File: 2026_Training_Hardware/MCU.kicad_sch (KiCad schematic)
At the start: 2 parts, among them J1 RJ45_LED_Shielded, U1 Teensy4.1_DEV-16771

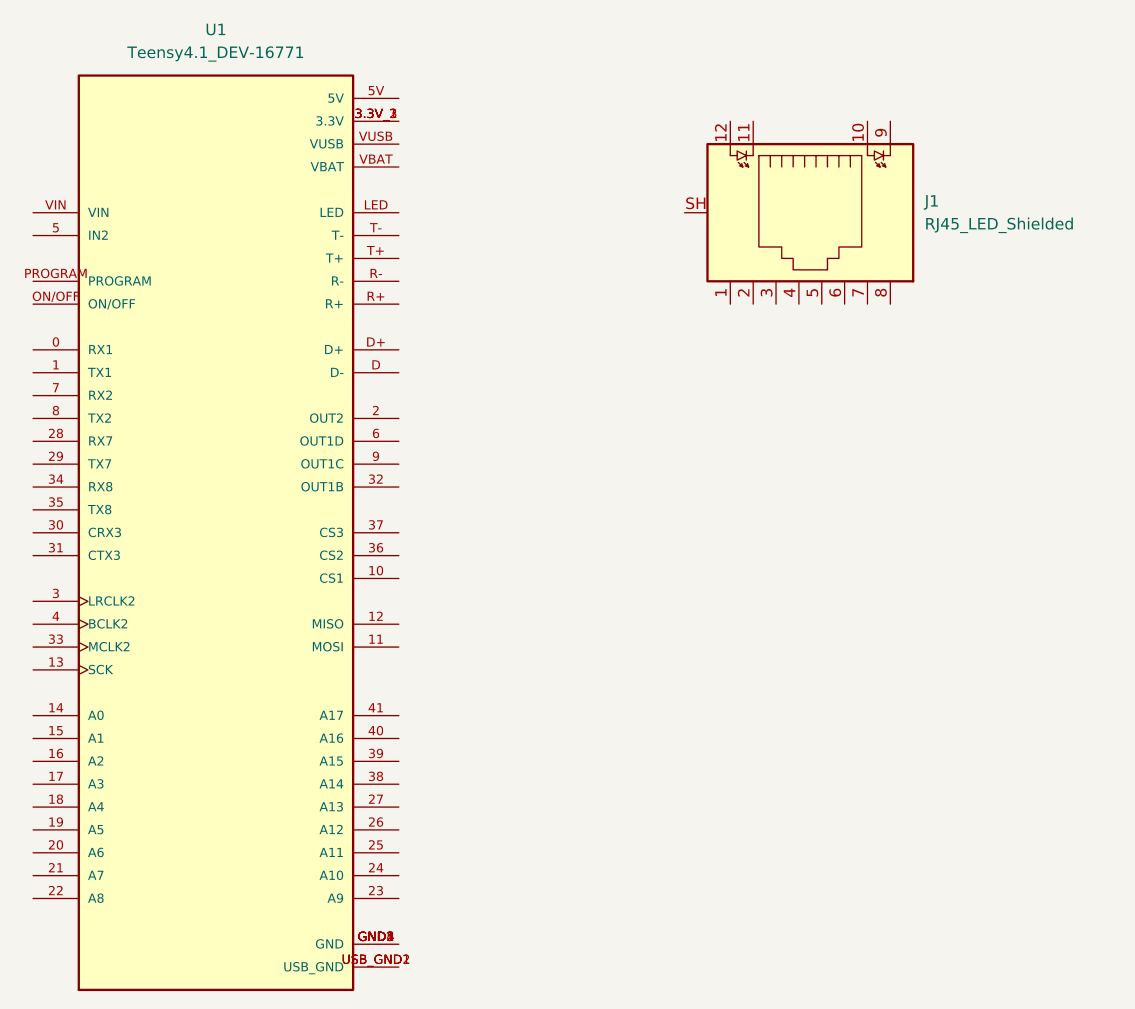
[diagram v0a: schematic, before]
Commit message: Add Ethernet
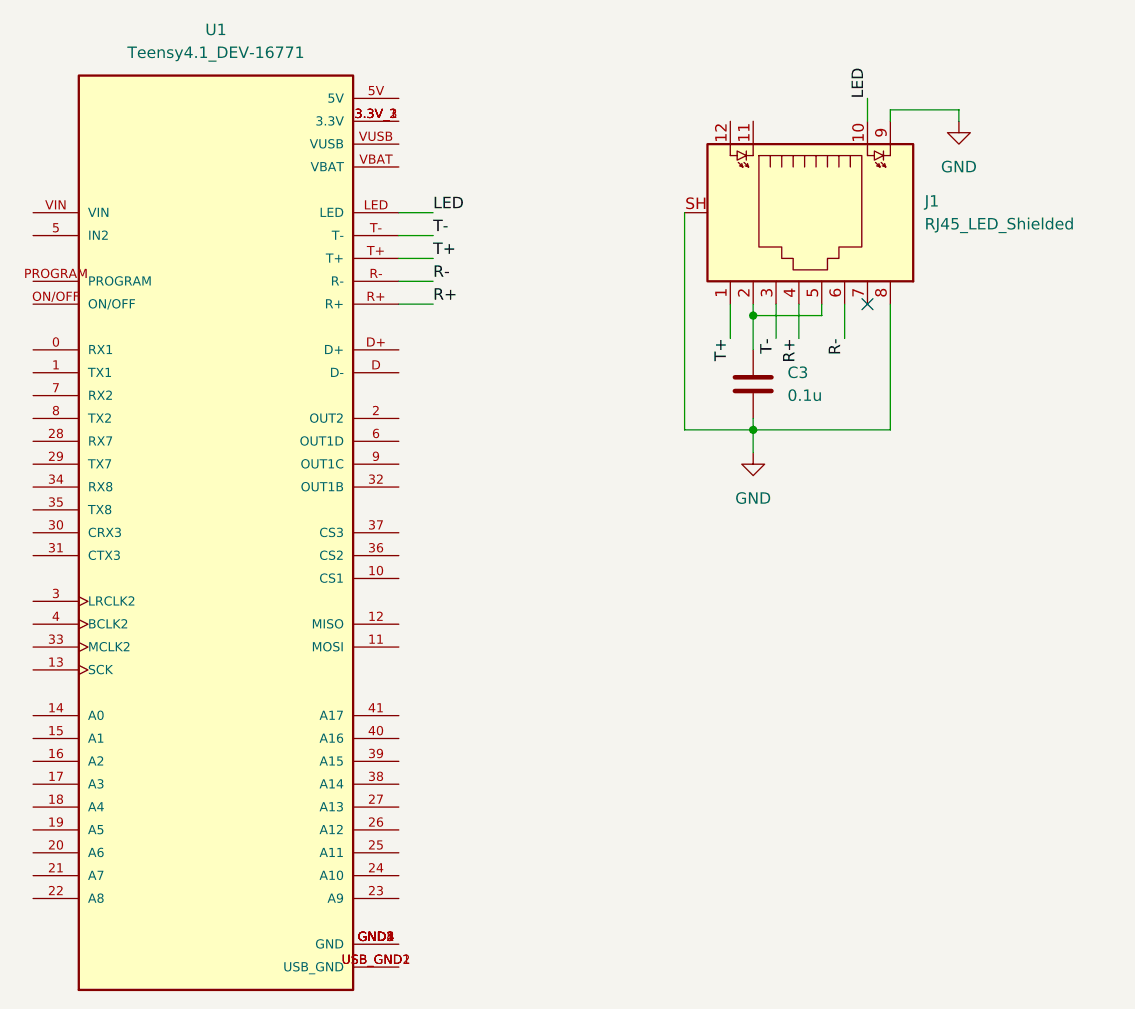
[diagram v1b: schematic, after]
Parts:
- added C3: 0.1u, symbol Device:C
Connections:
- net T+: now reaches J1.1
- net T+: now also U1.T+
- net LED: now reaches J1.10
- net LED: now also U1.LED
- net at J1.2: now also J1.5, C3.1
- net T-: now reaches J1.3
- net T-: now also U1.T-
- net R+: now reaches J1.4
- net R+: now also U1.R+
- net R-: now reaches J1.6
- net R-: now also U1.R-
- net GND: now reaches J1.8
- net GND: now also J1.9, J1.SH, C3.2
- no-connect marks 0 -> 1
